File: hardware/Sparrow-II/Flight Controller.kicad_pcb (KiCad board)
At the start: 4 copper layers, 41 x 41 mm, 103 parts

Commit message: hardware: layout checkpoint 3 - fixed DRC
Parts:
- removed R_HSE1: 0R, Resistor_SMD:R_0402_1005Metric
- moved R_FLASH_CS1 2.87 mm to (161.0, 99.8), turned to 180 degrees
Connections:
- net /Interfaces&IO/USB_C_DM renamed /Interfaces&IO/USB_C_DN
- net /Interfaces&IO/USB_DM renamed /Interfaces&IO/USB_DN
- C_OSD_XTAL2 pad 2: Net-(C_OSD_XTAL2-Pad2) -> /Video&OSD/OSD_CLK_OUT
- Y_OSD1 pad 1: Net-(C_OSD_XTAL2-Pad2) -> /Video&OSD/OSD_CLK_OUT
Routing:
- added copper zone on In1.Cu, net GND
- added copper zone on In2.Cu, net GND
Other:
- rule pad_to_mask_clearance: 0 -> 0.02

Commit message: hardware: decoupling capacitors route
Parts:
- moved R_I2C_SCL1 10.5 mm to (152.8, 97.0)
- moved R_I2C_SDA1 7.62 mm to (152.5, 96.0)
- moved C_VDD2 3.59 mm to (147.2, 103.2), turned to -90 degrees
- moved R_BOOT0 3.32 mm to (145.5, 85.5)
- moved C_VDD_BULK1 1.77 mm to (149.8, 104.5)
- moved C_VDD1 0.66 mm to (144.2, 89.1), turned to 180 degrees
- moved JP_BOOT0 0.56 mm to (143.8, 85.5)
- turned C_VDD3 to 0 degrees
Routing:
- net +3V3: track 0.00 -> 9.17 mm, vias 0 -> 2
- net Net-(JP_BOOT0-B): track 0.00 -> 8.37 mm, vias 0 -> 1
- net GND: track 0.00 -> 7.09 mm, vias 0 -> 8
- net Net-(U_MCU1-VCAP_1): track 0.00 -> 5.94 mm
- net /MCU Core/NRST: track 0.00 -> 5.38 mm
- added copper zone on In2.Cu, net +3V3
- removed copper zone on In2.Cu, net GND

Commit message: hardware: mcu routed & buck in progress
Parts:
- D_TVS1: moved to F.Cu
- moved J_GPS1 13.0 mm to (157.0, 118.0)
- moved J_BAT1 9.50 mm to (145.2, 117.5)
- moved D_TVS1 6.75 mm to (143.2, 112.0), turned to 180 degrees
- moved C_BUCK_IN3 4.10 mm to (132.2, 108.1), turned to -90 degrees
- moved R_I2C_SDA1 3.25 mm to (149.2, 96.0)
- moved C_HSE1 3.17 mm to (138.8, 96.3)
- moved C_HSE2 2.26 mm to (138.8, 93.5)
- moved FB_IMU1 2.25 mm to (153.0, 97.8), turned to 0 degrees
- moved R_I2C_SCL1 2.25 mm to (150.5, 97.0)
- moved TP_5VIDEO_0 1.48 mm to (130.5, 99.5)
- moved C_BUCK_IN1 1.15 mm to (134.8, 108.9)
- moved Y_HSE1 1.15 mm to (141.2, 94.7)
- moved C_BUCK_BOOT1 1.12 mm to (131.8, 102.0)
- moved C_BUCK_IN2 1.10 mm to (138.0, 108.9)
- moved C_IMU_VDD2 1.00 mm to (153.0, 98.8)
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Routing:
- net GND: track 7.09 -> 60.6 mm, vias 8 -> 40
- net VBAT: track 0.00 -> 30.7 mm
- net /MCU Core/I2C1_SCL: track 0.00 -> 8.40 mm, vias 0 -> 1
- net /MCU Core/I2C1_SDA: track 0.00 -> 6.67 mm, vias 0 -> 1
- net /MCU Core/RCC_OSC_IN: track 0.00 -> 6.31 mm, vias 0 -> 1
- net +3V3: track 9.17 -> 15.3 mm, vias 2 -> 6
- net /MCU Core/IMU_CS: track 0.00 -> 5.82 mm, vias 0 -> 1
- net Net-(U_BUCK1-SS): track 0.00 -> 5.80 mm, vias 0 -> 1
- net /MCU Core/RCC_OSC_OUT: track 0.00 -> 4.83 mm, vias 0 -> 1
- net /MCU Core/SPI1_SCK: track 0.00 -> 4.50 mm, vias 0 -> 1
- net Net-(U_IMU1-VDD): track 0.00 -> 4.24 mm
- net Net-(C_HSE1-Pad2): track 0.00 -> 4.20 mm
- net /MCU Core/SPI1_MISO: track 0.00 -> 3.57 mm, vias 0 -> 1
- net Net-(U_BUCK1-BOOT): track 0.00 -> 3.03 mm
- net /MCU Core/IMU_INT: track 0.00 -> 2.84 mm, vias 0 -> 1
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
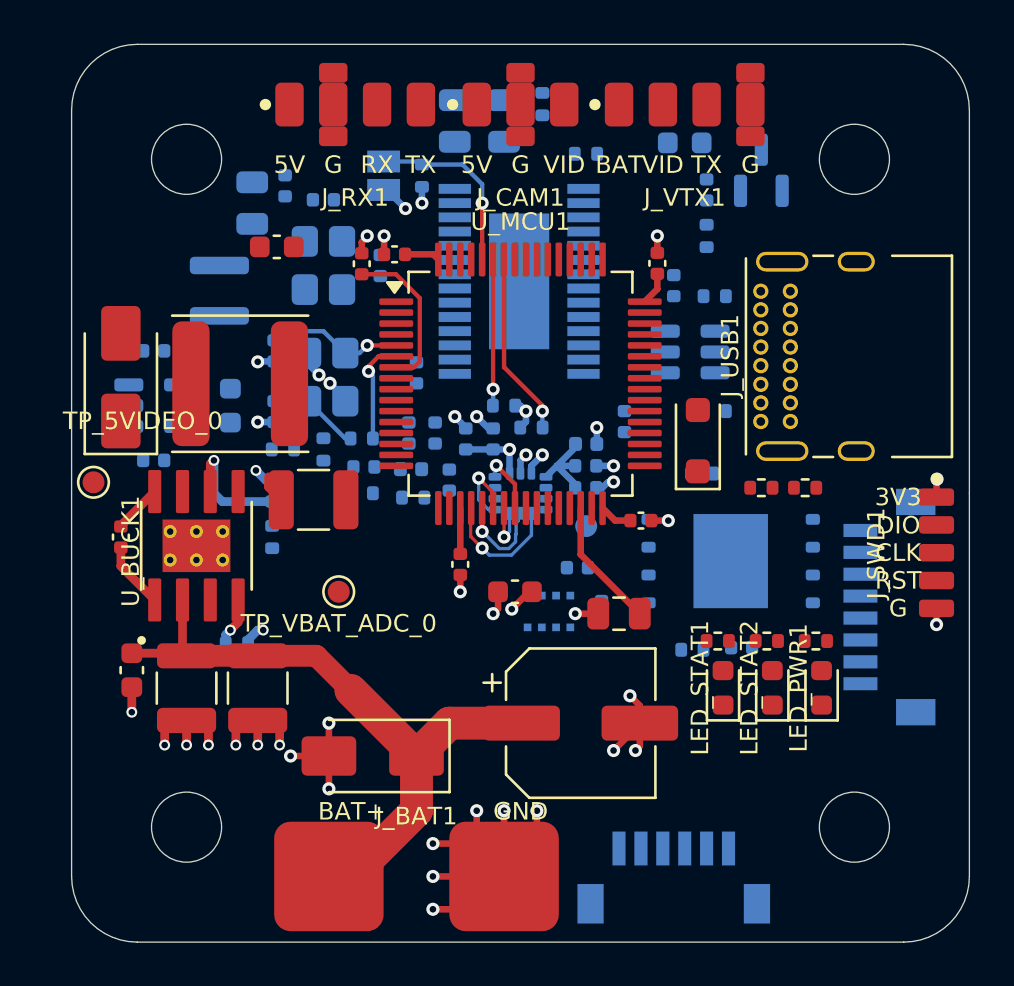
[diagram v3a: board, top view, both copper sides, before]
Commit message: hardware: buck, baro, blackbox, osd routed
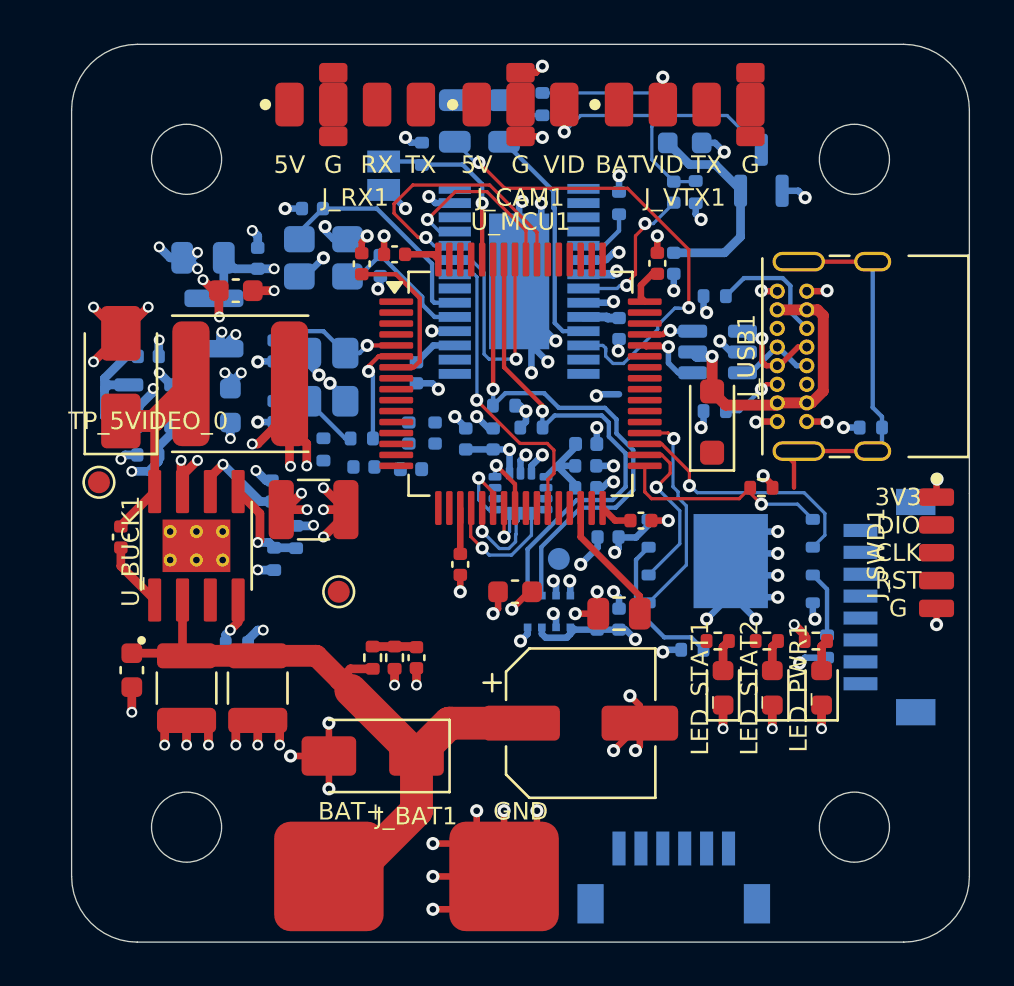
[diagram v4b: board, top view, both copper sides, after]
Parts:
- C_VBAT_ADC1, R_VBAT_D1, R_VBAT_D2: moved to F.Cu
- R_USB_SH1: moved to B.Cu
- moved R_FLASH_WP1 9.74 mm to (164.0, 107.0), turned to 90 degrees
- moved C_VBAT_ADC1 8.25 mm to (145.2, 107.5), turned to -90 degrees
- moved C_FLASH1 7.92 mm to (154.0, 102.0), turned to 180 degrees
- moved R_VBAT_D1 7.53 mm to (143.2, 107.5), turned to -90 degrees
- moved R_VBAT_D2 7.36 mm to (144.2, 107.5), turned to 90 degrees
- moved R_BUCK_FB2 5.02 mm to (138.8, 103.0), turned to -90 degrees
- moved C_OSD_PVDD2 4.26 mm to (154.5, 92.5)
- moved R_USB_SH1 4.07 mm to (166.0, 97.0), turned to 180 degrees
- moved C_VID3 3.54 mm to (138.0, 89.3)
- moved C_VID1 3.36 mm to (135.5, 89.2), turned to 180 degrees
- moved C_5V_BULK1 2.74 mm to (137.0, 90.8)
- moved R_OSD_RST1 2.71 mm to (154.5, 86.8), turned to -90 degrees
- moved C_BARO1 2.52 mm to (153.5, 105.8), turned to 90 degrees
- moved R_VID_IN_T1 2.06 mm to (158.0, 86.2)
- moved TP_IMU_INT_0 1.95 mm to (151.8, 103.0)
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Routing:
- net GND: track 60.6 -> 159.4 mm, vias 40 -> 109
- net +5V: track 1.29 -> 24.0 mm, vias 0 -> 9
- net Net-(U_OSD1-VOUT): track 0.00 -> 22.3 mm, vias 0 -> 2
- net +3V3: track 15.3 -> 35.5 mm, vias 6 -> 16
- net +5V_VIDEO: track 0.00 -> 17.9 mm, vias 0 -> 2
- net Net-(J_USB1-SHIELD): track 0.00 -> 17.7 mm
- net /MCU Core/I2C1_SDA: track 6.67 -> 24.1 mm
- net /Video&OSD/VIDEO_IN: track 0.00 -> 15.9 mm, vias 0 -> 1
- net /MCU Core/I2C1_SCL: track 8.40 -> 22.8 mm
- net /MCU Core/OSD_CS: track 0.00 -> 13.9 mm, vias 0 -> 1
- net /Interfaces&IO/+5V_USB: track 0.00 -> 13.8 mm, vias 0 -> 1
- net /MCU Core/SPI3_SCK: track 0.00 -> 12.8 mm, vias 0 -> 1
- net /MCU Core/SPI2_MISO: track 0.00 -> 11.7 mm, vias 0 -> 1
- net /MCU Core/SPI3_MOSI: track 0.00 -> 11.4 mm, vias 0 -> 1
- net Net-(U_OSD1-SAG): track 0.00 -> 10.7 mm
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
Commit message: hardware: checkpoint - 1 unrouted track
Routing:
- net VBAT: track 32.4 -> 138.6 mm, vias 0 -> 9
- net +3V3: track 35.5 -> 108.9 mm, vias 16 -> 28
- net +5V_VIDEO: track 17.9 -> 84.0 mm, vias 2 -> 4
- net /MCU Core/NRST: track 7.18 -> 51.5 mm, vias 0 -> 4
- net /Interfaces&IO/ESC_CURR_IN: track 0.00 -> 36.3 mm, vias 0 -> 2
- net /MCU Core/SWCLK: track 0.00 -> 31.3 mm, vias 0 -> 4
- net /Interfaces&IO/M4: track 0.00 -> 29.5 mm, vias 0 -> 2
- net +5V: track 24.0 -> 52.1 mm, vias 9 -> 3
- net /Interfaces&IO/ESC_TEL: track 0.00 -> 28.1 mm, vias 0 -> 3
- net /MCU Core/SWDIO: track 0.00 -> 26.0 mm, vias 0 -> 2
- net GND: track 159.4 -> 183.5 mm, vias 109 -> 121
- net /Interfaces&IO/RC_RX: track 0.00 -> 23.3 mm, vias 0 -> 2
- net /Interfaces&IO/GPS_TX: track 0.00 -> 21.3 mm, vias 0 -> 1
- net /MCU Core/I2C1_SCL: track 22.8 -> 42.0 mm
- net /Interfaces&IO/M3: track 0.00 -> 18.9 mm, vias 0 -> 4
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
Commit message: hardware: checkpoint - all routed
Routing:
- net +5V: track 52.1 -> 79.9 mm, vias 3 -> 7
- net /Interfaces&IO/ESC_TEL: track 28.1 -> 31.8 mm, vias 3 -> 2
- net +3V3: track 108.9 -> 110.2 mm, vias 28 -> 30
- net /Interfaces&IO/M1: track 15.3 -> 16.4 mm, vias 2 -> 3

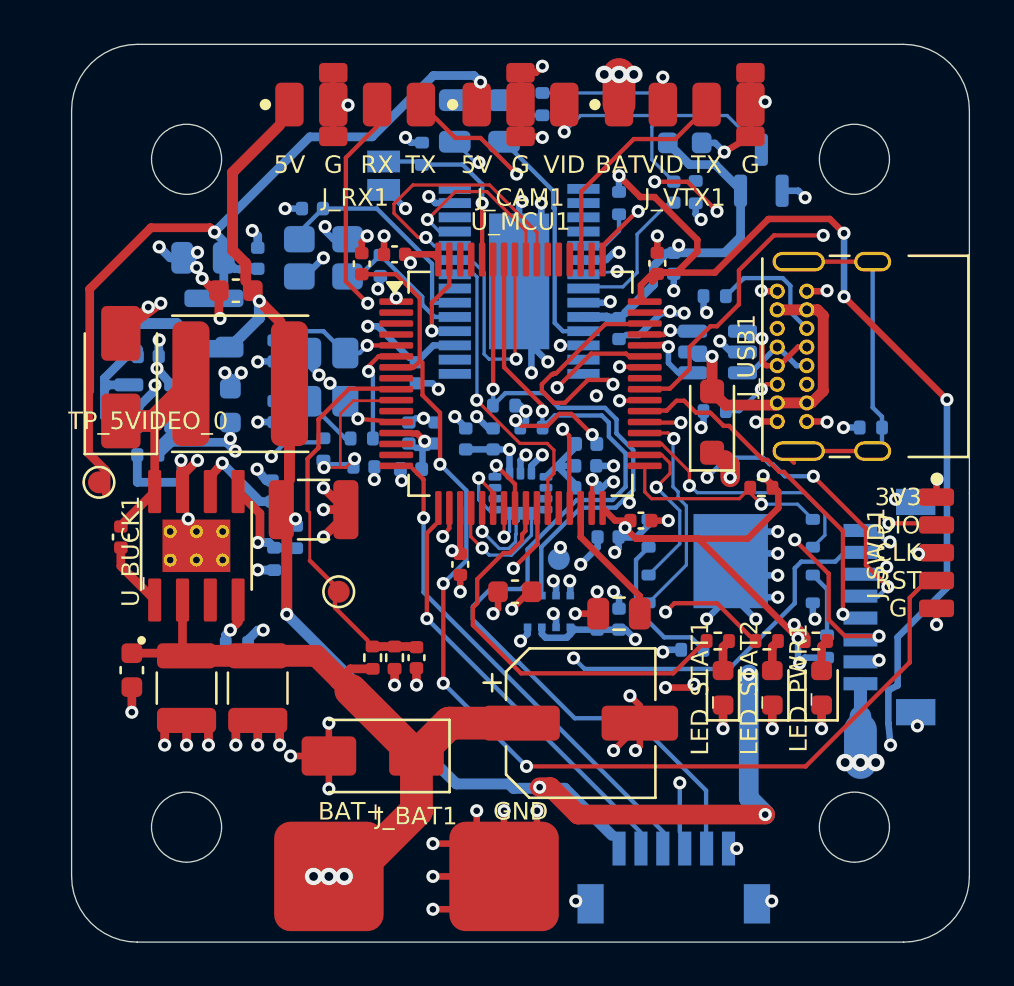
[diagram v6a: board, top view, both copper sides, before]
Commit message: hardware: Sparrow II routed
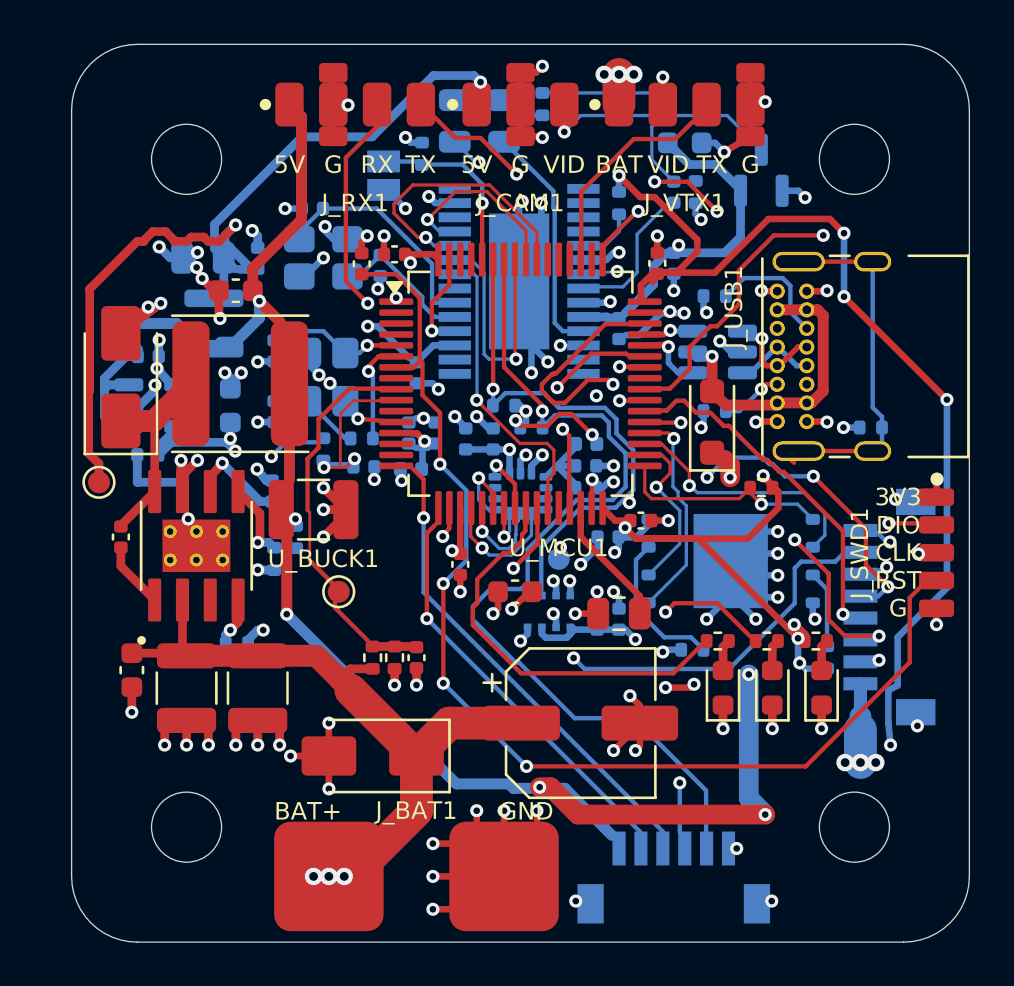
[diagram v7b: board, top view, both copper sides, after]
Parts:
- added LOGO1: Sparrowhawk_Logo, Sparrowhawk_Logo, B.Cu at (146.0, 113.8)
- moved R_FLASH_WP1 0.50 mm to (164.0, 107.5)
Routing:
- net +5V_VIDEO: track 84.0 -> 85.6 mm
- net +5V: track 79.9 -> 81.3 mm
- net Net-(U_FLASH1-~{WP}/IO_{2}): track 3.02 -> 3.52 mm
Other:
- board text added: "v1.0"
